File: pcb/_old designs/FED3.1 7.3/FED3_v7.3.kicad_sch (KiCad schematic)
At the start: 29 parts, among them IC2 TB6612FNG, SW1 Sw, U2 MIC5504-3.3, U3 MCP73831T, X5 JST-XH-02

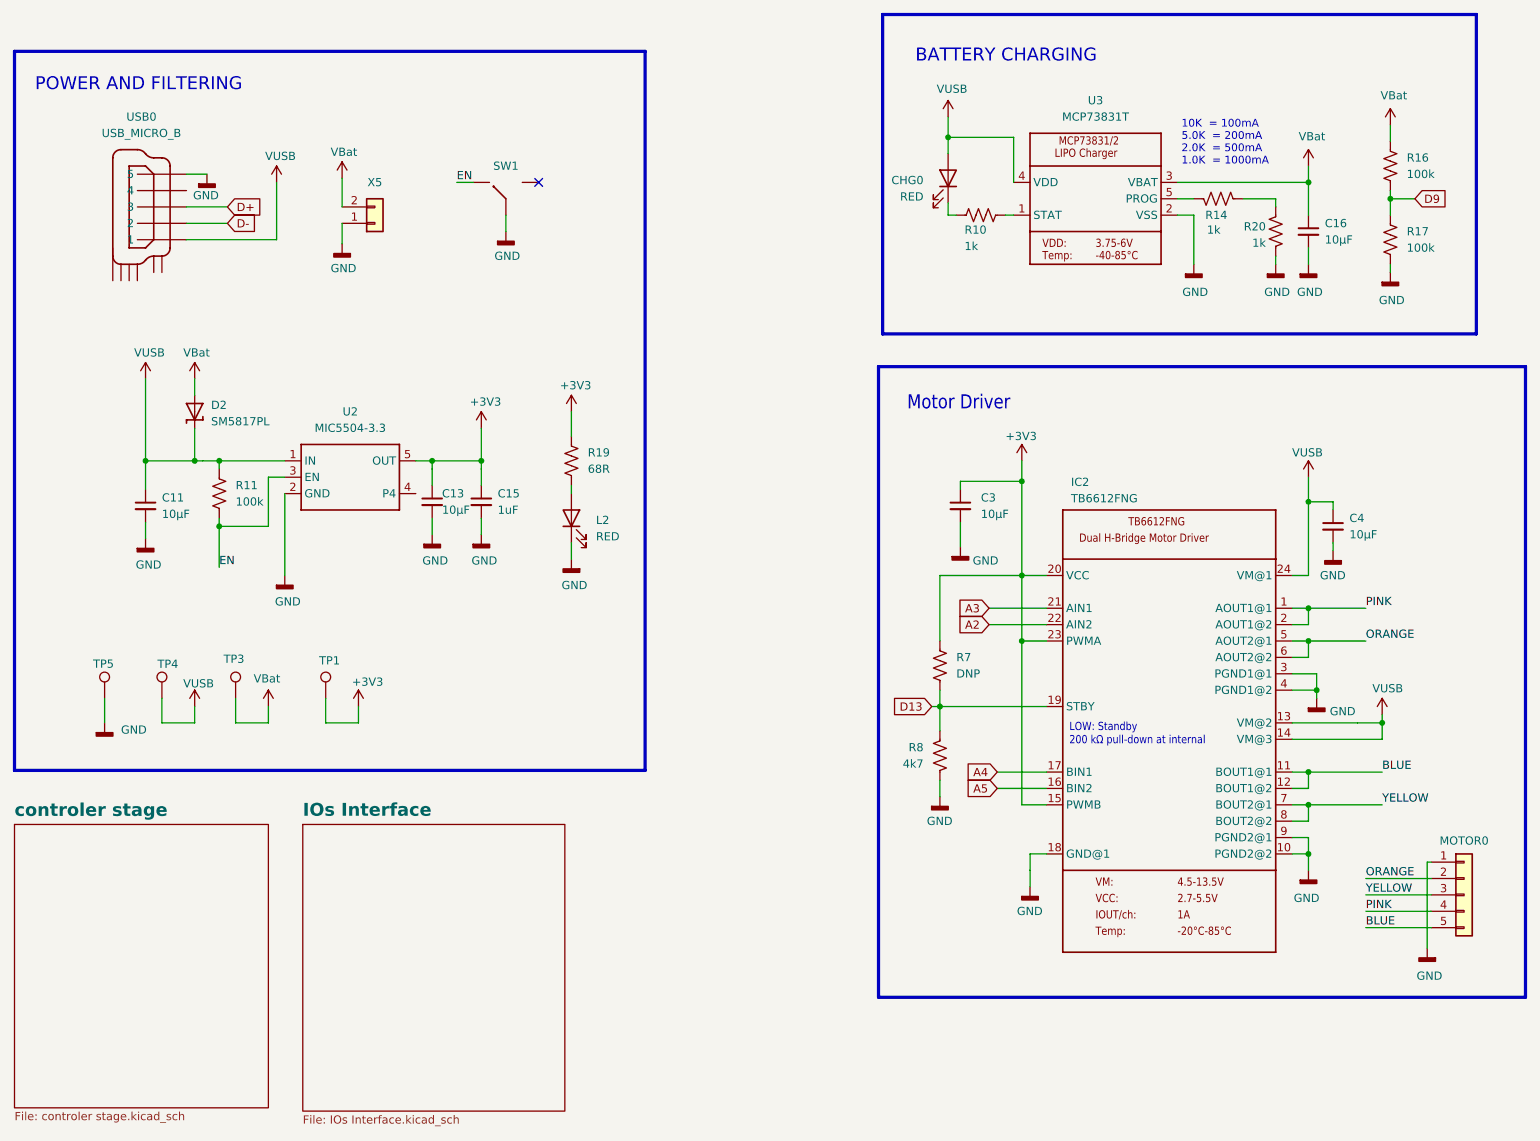
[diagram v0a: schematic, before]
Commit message: v.7.4 - alterações rail power
v.7.4
- modificada estrutura rail power: VUSB apenas para Vcharging
- modificadas Rs de LEDs para diminuir I
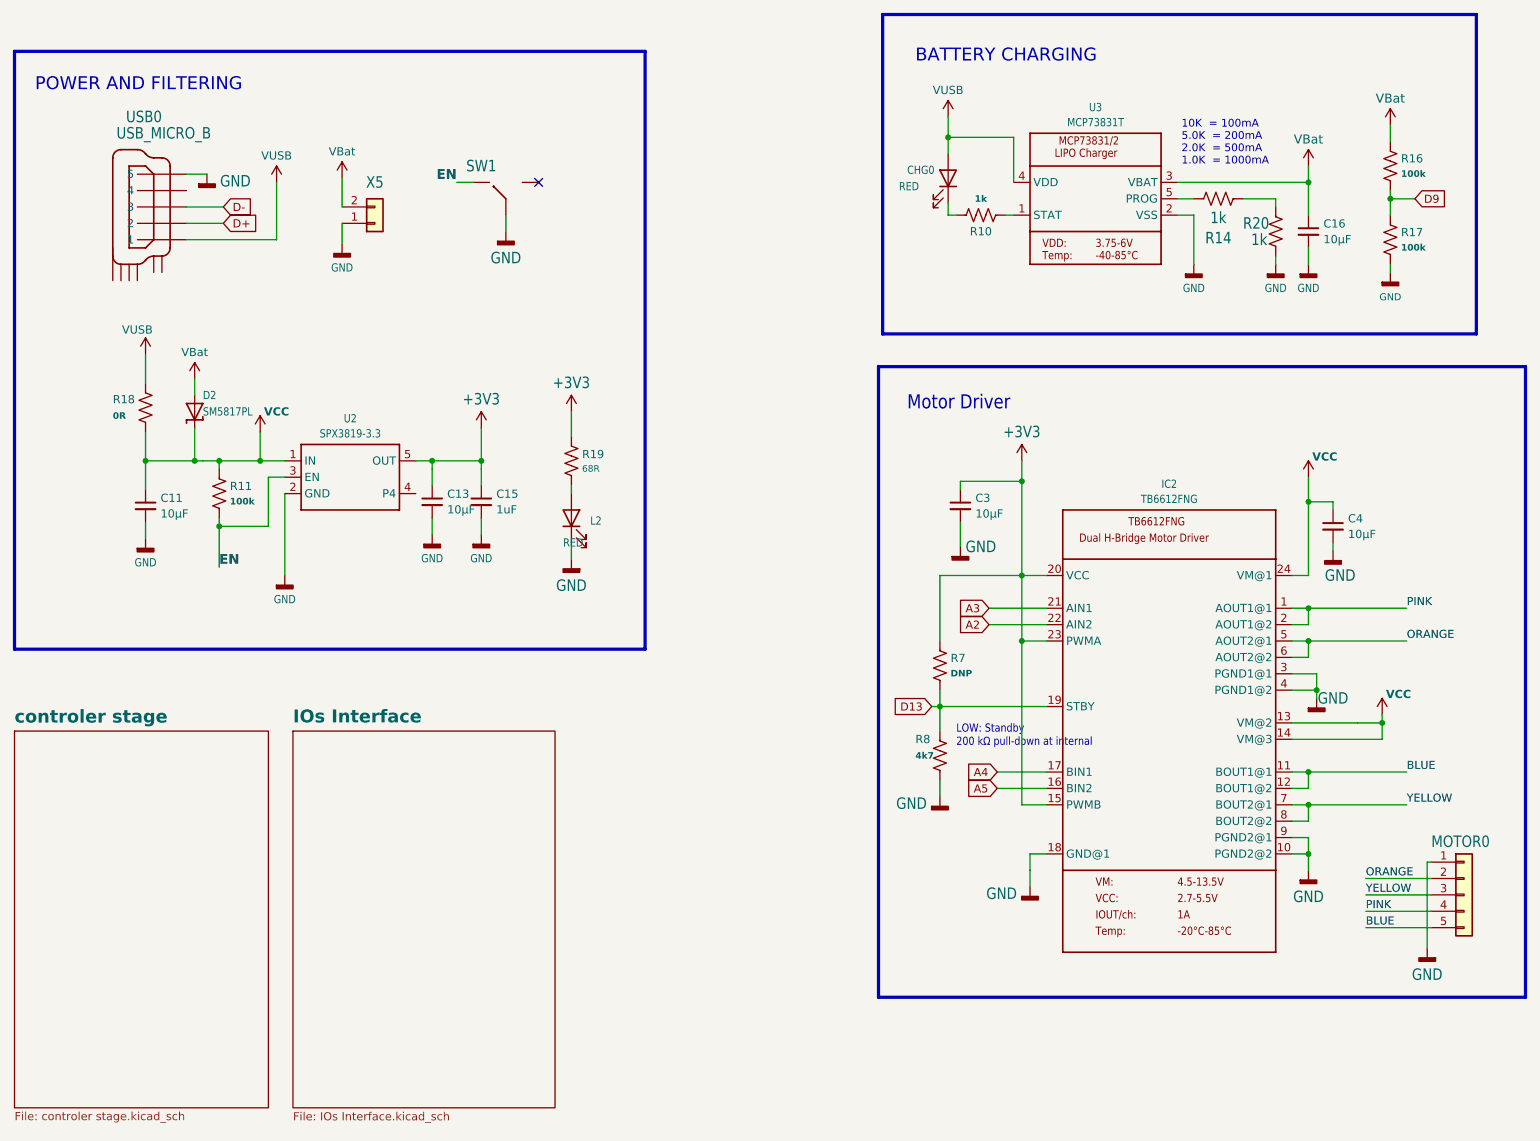
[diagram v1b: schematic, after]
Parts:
- removed TP1: 3V3, TestPoint:TestPoint_Pad_1.0x1.0mm, symbol Connector:TestPoint
- removed TP3: VBat, TestPoint:TestPoint_Pad_1.0x1.0mm, symbol Connector:TestPoint
- removed TP4: VUSB, TestPoint:TestPoint_Pad_1.0x1.0mm, symbol Connector:TestPoint
- removed TP5: GND, TestPoint:TestPoint_THTPad_2.0x2.0mm_Drill1.0mm, symbol Connector:TestPoint
- added R18: 0R, Resistor_SMD:R_0402_1005Metric, symbol Device:R_US
- CHG0, L2: MPN 5975004407F -> VFHR1116P-4C82A-TR; OEPSPN OEPS030006 -> OEPS030038
- D2: symbol FED3 SymbLib:DIODE-SCHOTTKYSOD-123 -> FED3_v7.3 SymLib:DIODE-SCHOTTKYSOD-123
- IC2: footprint FED3_PCBLib:SSOP24 -> FED3_v7.3:SSOP24; symbol FED3 SymbLib:TB6612FNGSSOP -> FED3_v7.3 SymLib:TB6612FNGSSOP
- MOTOR0: footprint FED3_PCBLib:1X05 -> FED3_v7.3:1X05
- SW1: footprint FED3_PCBLib:SSSS811101 -> FED3_v7.3:SSSS811101; symbol FED3 SymbLib:SSSS811101 -> FED3_v7.3 SymLib:SSSS811101
- U2: value MIC5504-3.3 -> SPX3819-3.3; symbol FED3 SymbLib:VREG_SOT23-5 -> FED3_v7.3 SymLib:VREG_SOT23-5; MPN MIC5504-3.3YM5-TR -> SPX3819-3.3; OEPSPN OEPS080052 -> OEPS080165
- U3: symbol FED3 SymbLib:MCP73831/2 -> FED3_v7.3 SymLib:MCP73831/2
- USB0: footprint FED3_PCBLib:ZX62D-B-5P8 -> FED3_v7.3:ZX62D-B-5P8; symbol FED3 SymbLib:USB_MICRO_B -> FED3_v7.3 SymLib:USB_MICRO_B
- X5: footprint FED3_PCBLib:JST-XH-02-PACKAGE-ROUND-PAD -> FED3_v7.3:JST-XH-02-PACKAGE-ROUND-PAD
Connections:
- net D+: now also USB0.P$2 (2); no longer USB0.P$3 (3)
- net D-: now also USB0.P$3 (3); no longer USB0.P$2 (2)
- net VUSB: now also R18.1; no longer C11.1, C4.1, D2.1 (K), IC2.13 (VM@2), IC2.14 (VM@3), IC2.24 (VM@1), R11.1, U2.1 (IN)
- new net VCC: C11.1, C4.1, D2.1 (K), IC2.13 (VM@2), IC2.14 (VM@3), IC2.24 (VM@1), R11.1, R18.2, U2.1 (IN)
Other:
- moved on the sheet: R20, R8
